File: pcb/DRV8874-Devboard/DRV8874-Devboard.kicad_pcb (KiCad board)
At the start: 4 copper layers, 65 x 67 mm, 57 parts, among them J1 Conn_01x04_Pin, J10 Conn_01x06_Pin, J12 Conn_01x03_Pin, J2 Screw_Terminal_01x02, J3 Conn_01x03_Pin, J4 Conn_01x03_Pin, J5 Conn_01x04_Pin, J6 Conn_01x03_Pin, J7 Conn_01x03_Pin, J8 Conn_01x03_Pin, J9 Conn_01x03_Pin, U1 DRV8874, U2 BL9342, U3 DRV8874, U4 SN65HVD230, U5 TPS16630PWPR, U6 M95320-WMN6TP, U7 TinyThinker_J1

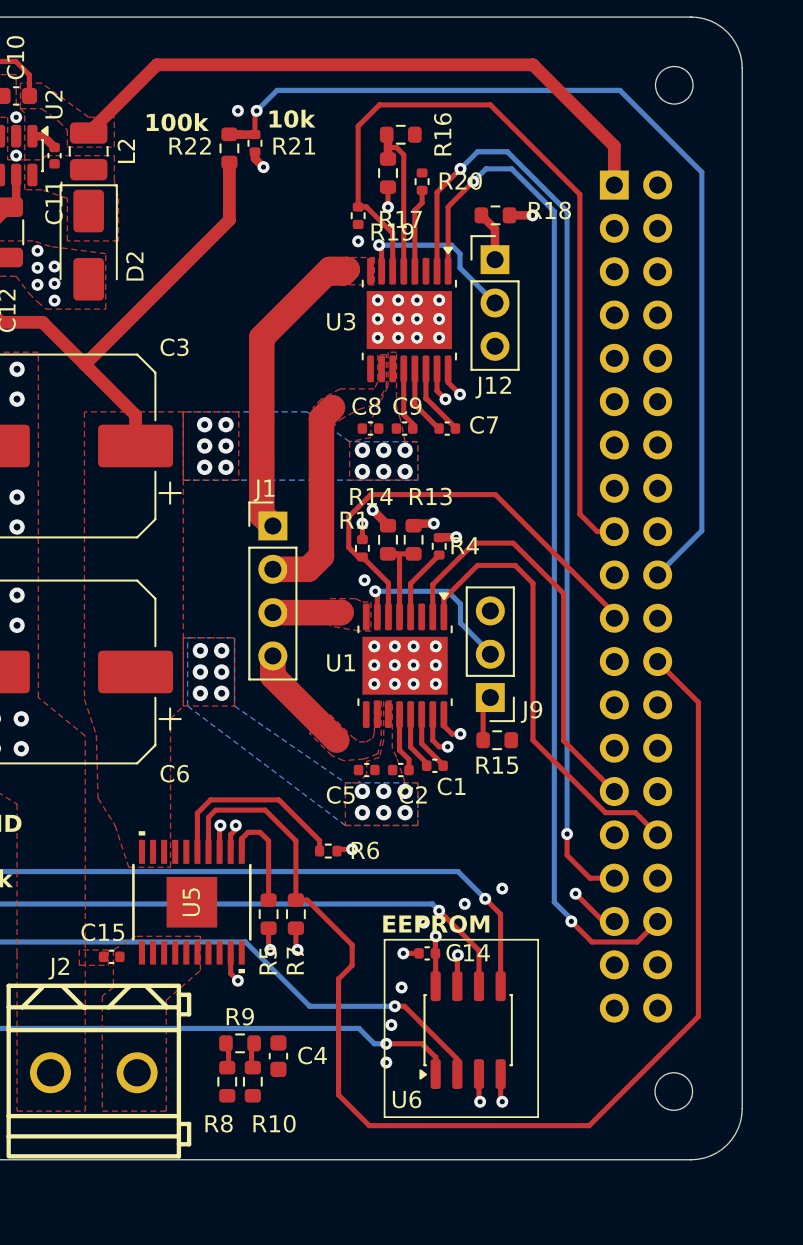
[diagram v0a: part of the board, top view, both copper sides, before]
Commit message: minor routing changes
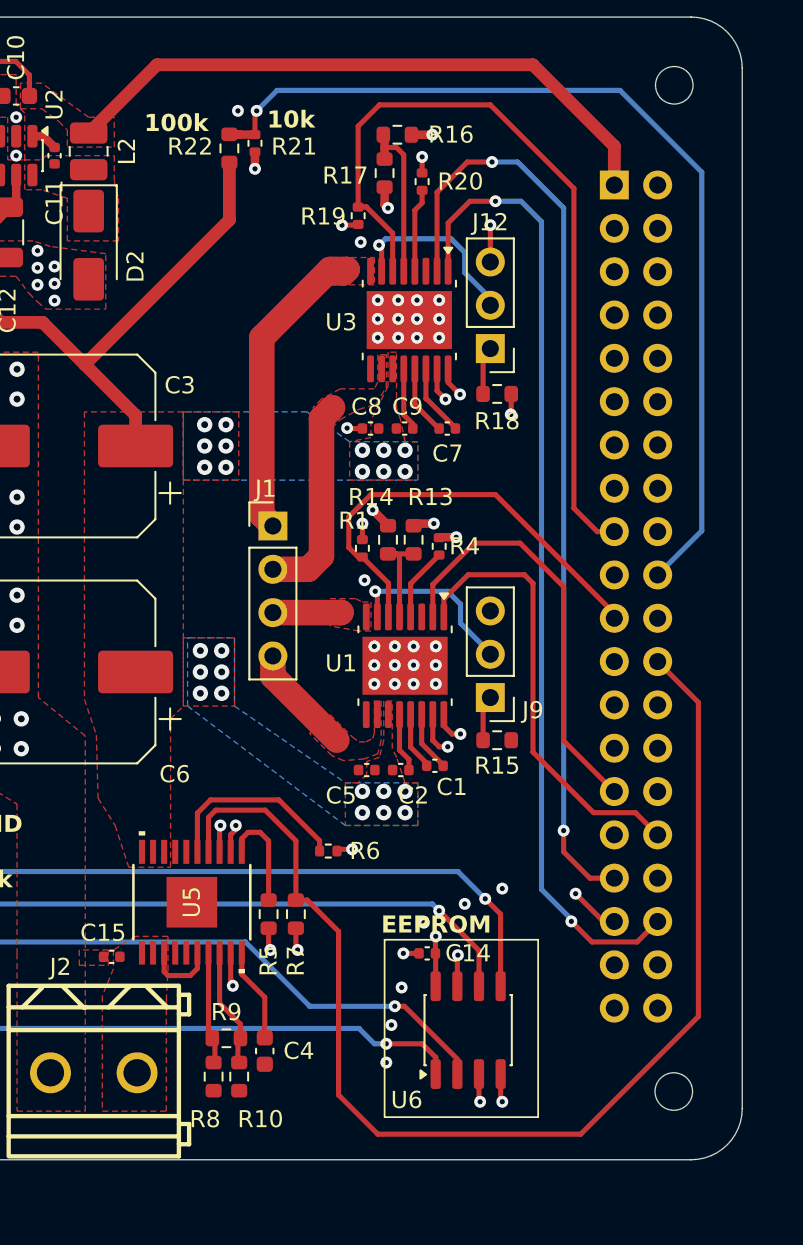
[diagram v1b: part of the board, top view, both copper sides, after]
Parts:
- moved R18 10.5 mm to (147.4, 61.7)
- moved J12 5.22 mm to (147.0, 59.0), turned to 180 degrees
- moved C4 0.85 mm to (133.8, 100.2)
- moved R10 0.85 mm to (132.3, 101.7)
- moved R8 0.85 mm to (130.8, 101.7)
- moved R9 0.85 mm to (131.5, 99.5)
- moved R16 0.20 mm to (141.6, 46.5)
- moved R17 0.20 mm to (140.8, 48.8)
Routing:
- net /TPS_DVDT: track 0.00 -> 5.56 mm
- net /TPS_OVP: track 1.56 -> 7.09 mm
- net /TPS_UVLO: track 1.85 -> 6.68 mm
- net +BATT_RAW: track 0.00 -> 4.27 mm
- net GND: track 29.0 -> 33.0 mm, vias 91 -> 94
- net /B_IN1: track 60.1 -> 57.1 mm
- net +3.3V: track 16.7 -> 18.8 mm, vias 10 -> 12
- net /B_IMODE: track 10.3 -> 10.8 mm

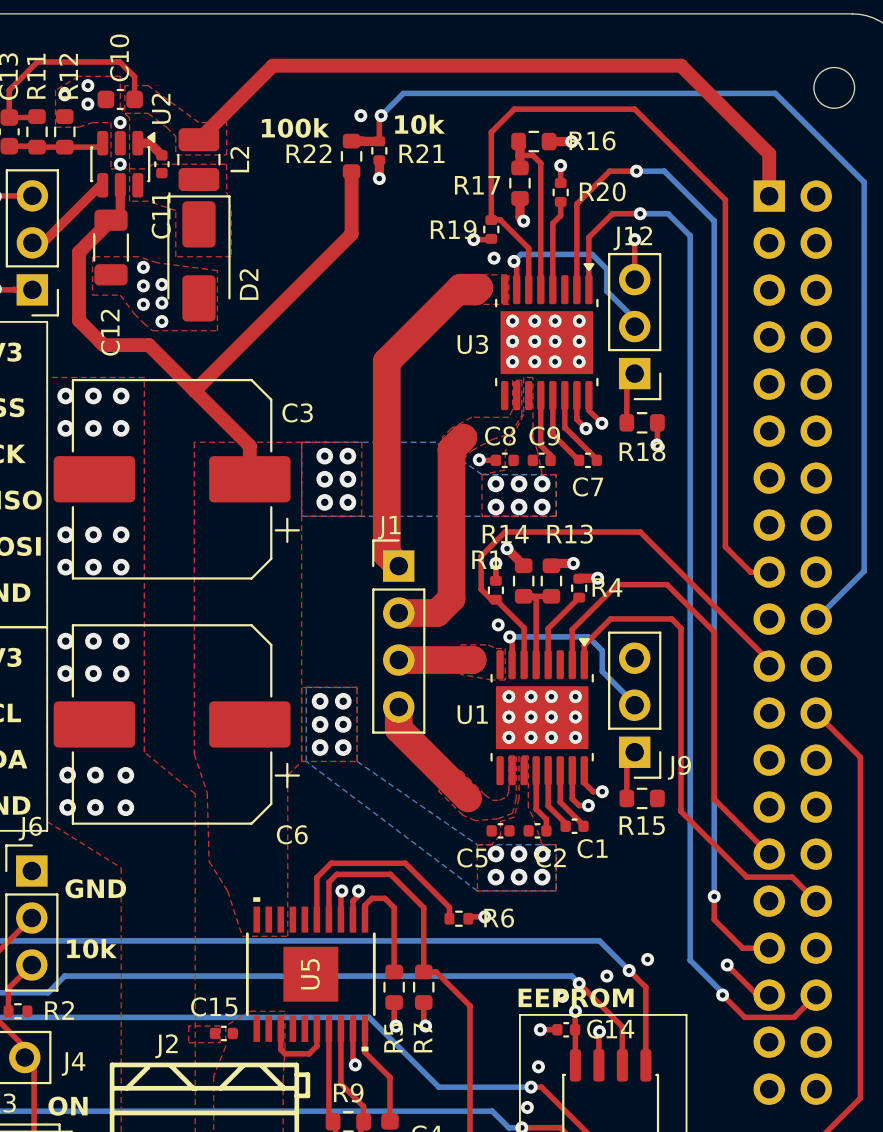
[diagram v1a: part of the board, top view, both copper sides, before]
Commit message: minor routing changes
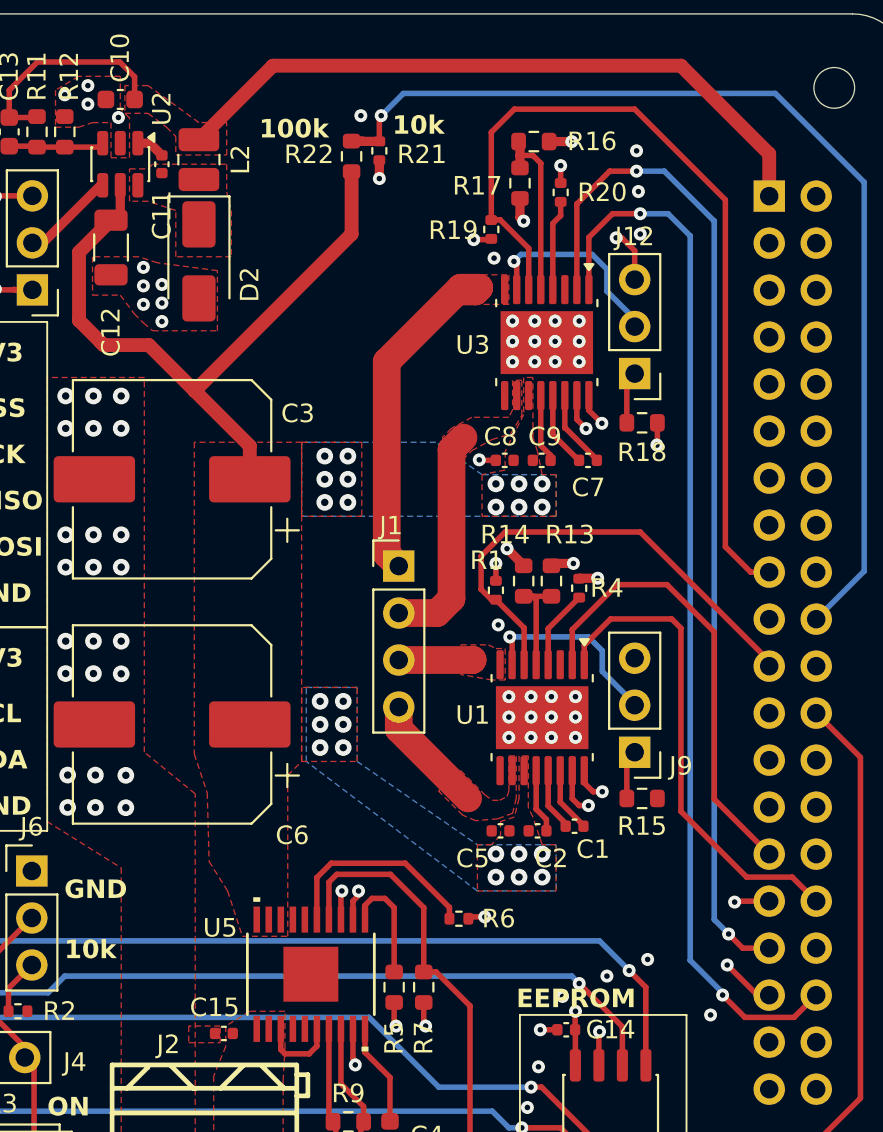
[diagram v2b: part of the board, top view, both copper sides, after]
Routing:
- net GND: track 33.0 -> 35.6 mm, vias 94 -> 98
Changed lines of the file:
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@@
 		(tags "TPS16630PWPR ")
 		(property "Reference" "U5"
-			(at 0 0 90)
+			(at 2.5 -4.9 0)
 			(unlocked yes)
 			(layer "F.SilkS")
@@
 	)
 	(segment
-		(start 147 53.96)
-		(end 147 51.8)
-		(width 0.3)
-		(layer "F.Cu")
-		(net 2)
-	)
-	(segment
 		(start 114.45 54.515)
 		(end 112.49 54.515)
@@
 	)
 	(segment
+		(start 146 51.7)
+		(end 146.3 51.7)
+		(width 0.3)
+		(layer "F.Cu")
+		(net 2)
+	)
+	(segment
 		(start 112 102)
 		(end 111.25 102.75)
@@
 	)
 	(segment
+		(start 152.45 87.55)
+		(end 152.4 87.6)
+		(width 0.3)
+		(layer "F.Cu")
+		(net 2)
+	)
+	(segment
 		(start 143.625 82.01)
 		(end 143.625 80.4975)
@@
 	)
 	(segment
+		(start 154.27 87.55)
+		(end 152.45 87.55)
+		(width 0.3)
+		(layer "F.Cu")
+		(net 2)
+	)
+	(segment
 		(start 113.49 54.515)
 		(end 113.45 54.475)
@@
 	)
 	(segment
+		(start 146.3 51.7)
+		(end 147 52.4)
+		(width 0.3)
+		(layer "F.Cu")
+		(net 2)
+	)
+	(segment
+		(start 147 52.4)
+		(end 147 53.96)
+		(width 0.3)
+		(layer "F.Cu")
+		(net 2)
+	)
+	(segment
 		(start 143.875 61.515923)
 		(end 144.371183 62.012106)
@@
 	)
 	(via
+		(at 152.4 87.6)
+		(size 0.7)
+		(drill 0.3)
+		(layers "F.Cu" "B.Cu")
+		(net 2)
+	)
+	(via
 		(at 119.5 82.5)
 		(size 0.9)
@@
 	)
 	(via
+		(at 151.1 93.7)
+		(size 0.7)
+		(drill 0.3)
+		(layers "F.Cu" "B.Cu")
+		(net 2)
+	)
+	(via
 		(at 138.3 51.8)
 		(size 0.7)
@@
 	)
 	(via
+		(at 147.2 49.2)
+		(size 0.7)
+		(drill 0.3)
+		(layers "F.Cu" "B.Cu")
+		(net 2)
+	)
+	(via
 		(at 152 91)
 		(size 0.7)
@@
 	)
 	(via
+		(at 147.3 51.5)
+		(size 0.7)
+		(drill 0.3)
+		(layers "F.Cu" "B.Cu")
+		(net 2)
+	)
+	(via
 		(at 144 57.3)
 		(size 0.7)
@@
 	)
 	(via
+		(at 147.1 47)
+		(size 0.7)
+		(drill 0.3)
+		(layers "F.Cu" "B.Cu")
+		(net 2)
+	)
+	(via
 		(at 142.7 58.4)
 		(size 0.7)
@@
 	)
 	(via
-		(at 119.2 45.475)
+		(at 119.1 45.2)
 		(size 0.7)
 		(drill 0.3)
@@
 	)
 	(via
-		(at 147 51.8)
+		(at 146 51.7)
 		(size 0.7)
 		(drill 0.3)
@@
 	)
 	(via
-		(at 119.2 47.725)
-		(size 0.7)
-		(drill 0.3)
-		(layers "F.Cu" "B.Cu")
-		(free yes)
-		(net 2)
-	)
-	(via
 		(at 119.25 73.5)
 		(size 0.9)
@@
 	)
 	(segment
-		(start 151.3 88.55)
-		(end 152.84 90.09)
-		(width 0.3)
-		(layer "F.Cu")
-		(net 64)
-	)
-	(segment
 		(start 152.84 90.09)
 		(end 154.27 90.09)
@@
 	)
 	(segment
-		(start 151.3 87.3)
-		(end 151.3 88.55)
+		(start 145.65 48.1)
+		(end 143.875 49.875)
 		(width 0.3)
 		(layer "F.Cu")
@@
 	)
 	(segment
-		(start 145.65 48.1)
-		(end 143.875 49.875)
+		(start 152.075 89.325)
+		(end 152.84 90.09)
 		(width 0.3)
 		(layer "F.Cu")
@@
 	)
 	(via
-		(at 151.3 87.3)
+		(at 152.075 89.325)
 		(size 0.7)
 		(drill 0.3)
@@
 	)
 	(segment
-		(start 147.1 48.1)
-		(end 148.6 48.1)
+		(start 152.075 89.325)
+		(end 151.3 88.55)
 		(width 0.3)
 		(layer "B.Cu")
@@
 	(segment
 		(start 148.6 48.1)
+		(end 147.1 48.1)
+		(width 0.3)
+		(layer "B.Cu")
+		(net 64)
+	)
+	(segment
+		(start 151.3 88.55)
 		(end 151.3 50.8)
 		(width 0.3)
@@
 	(segment
 		(start 151.3 50.8)
-		(end 151.3 87.3)
+		(end 148.6 48.1)
 		(width 0.3)
 		(layer "B.Cu")
@@
 		(polygon
 			(pts
-				(xy 118.7 47.975) (xy 119.7 47.975) (xy 119.7 45.225) (xy 119.2 44.725) (xy 119.2 42.975) (xy 116.95 42.975)
+				(xy 118.7 47.375) (xy 119.7 47.375) (xy 119.7 45.225) (xy 119.2 44.725) (xy 119.2 42.975) (xy 116.95 42.975)
 				(xy 115.7 43.725) (xy 115.7 45.725) (xy 116.95 45.725) (xy 117.7 45.475) (xy 118.7 45.475)
 			)

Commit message: more minor routing cleanup
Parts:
- moved R6 0.83 mm to (137.1, 89.2)
- moved R19 0.78 mm to (138.7, 50.7), turned to 180 degrees
- moved R13 0.55 mm to (142.5, 69.7)
- moved R4 0.39 mm to (143.8, 70.3)
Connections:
- U7 pad 12: unconnected-(U7A-TIM3_CH1-Pad12) -> /A_IN1
- U7 pad 29: /A_IN2 -> unconnected-(U7A-TIM2_CH4-Pad29)
- U7 pad 32: /A_IN1 -> unconnected-(U7A-TIM2_CH1-Pad32)
- U7 pad 33: /B_IN2 -> unconnected-(U7A-TIM2_CH2-Pad33)
- U7 pad 36: /B_IN1 -> unconnected-(U7A-TIM2_CH3-Pad36)
- U7 pad 5: unconnected-(U7A-TIM3_CH4-Pad5) -> /B_IN2
- U7 pad 8: unconnected-(U7A-TIM3_CH3-Pad8) -> /B_IN1
- U7 pad 9: unconnected-(U7A-TIM3_CH2-Pad9) -> /A_IN2
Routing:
- net GND: track 35.6 -> 93.8 mm, vias 98 -> 140
- net /B_IN1: track 57.1 -> 18.4 mm
- net /B_IN2: track 55.3 -> 19.2 mm
- net +3.3V: track 18.8 -> 51.9 mm, vias 12 -> 30
- net /A_IN1: track 26.3 -> 21.2 mm, vias 0 -> 2
- net +BATT_RAW: track 4.27 -> 9.19 mm
- net /A_IN2: track 24.9 -> 20.6 mm, vias 0 -> 2
- net /A_IMODE: track 10.5 -> 13.4 mm
- net /B_IPROPI: track 46.3 -> 48.7 mm
- net /ADC_VSENSE: track 56.7 -> 58.6 mm
- net /TPS_MON: track 71.2 -> 72.3 mm

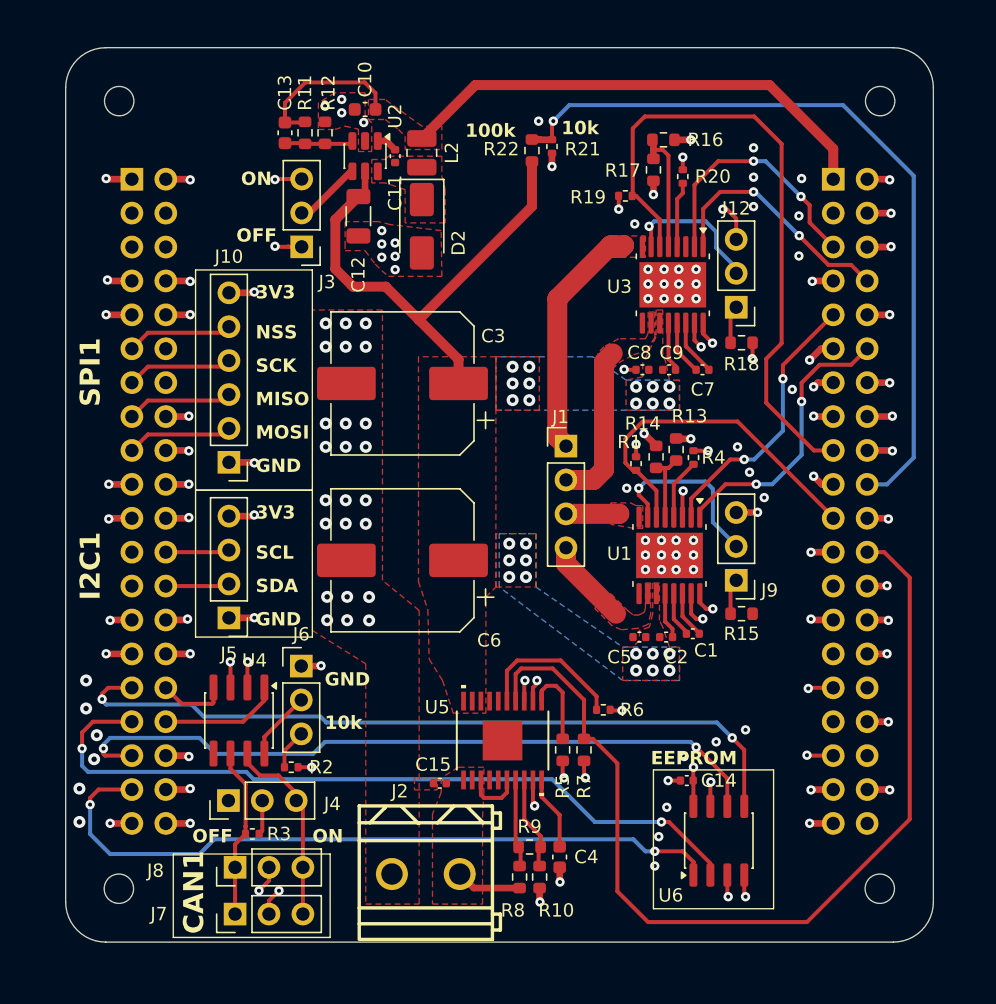
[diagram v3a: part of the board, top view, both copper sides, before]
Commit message: added 4 WS2812B RGB LEDs for status codes
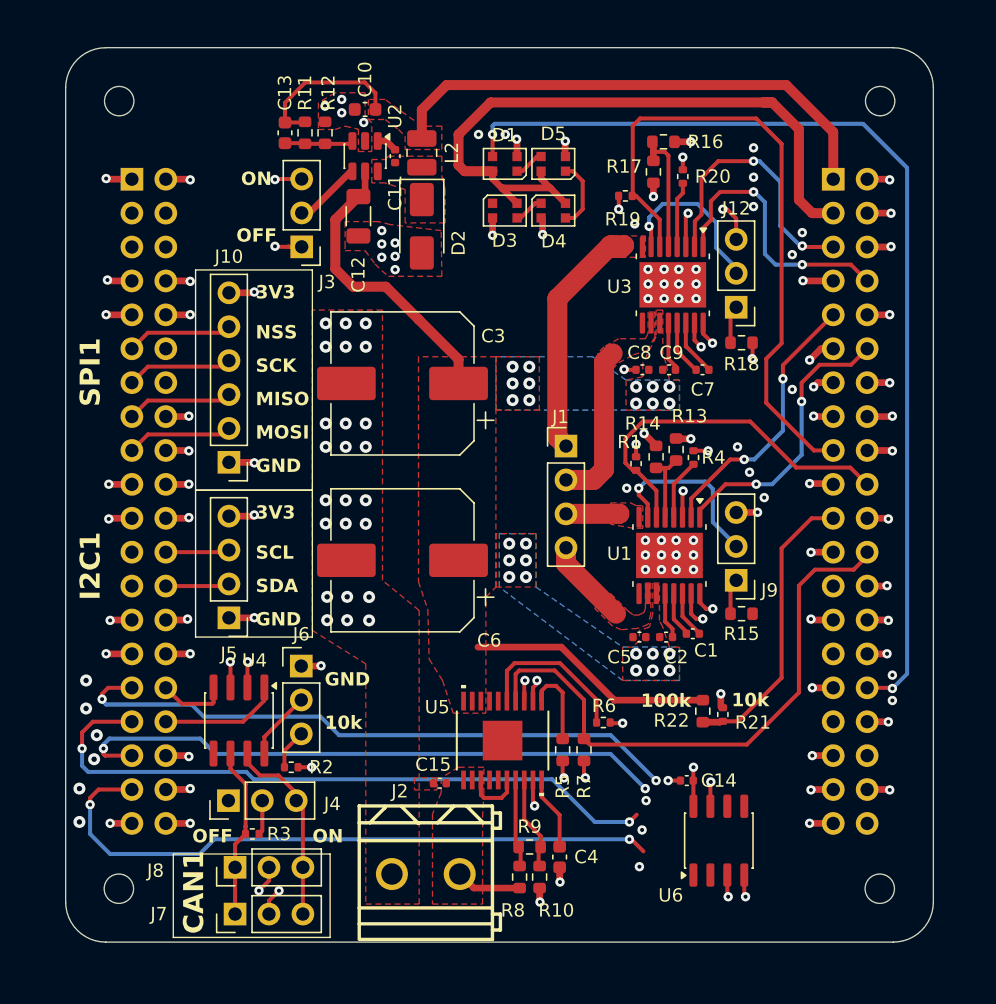
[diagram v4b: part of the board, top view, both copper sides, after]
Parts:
- added D1: WS2812B-2020, LED_SMD:LED_WS2812B-2020_PLCC4_2.0x2.0mm, F.Cu at (129.7, 48.3)
- added D3: WS2812B-2020, LED_SMD:LED_WS2812B-2020_PLCC4_2.0x2.0mm, F.Cu at (129.7, 51.8)
- added D4: WS2812B-2020, LED_SMD:LED_WS2812B-2020_PLCC4_2.0x2.0mm, F.Cu at (133.3, 51.8)
- added D5: WS2812B-2020, LED_SMD:LED_WS2812B-2020_PLCC4_2.0x2.0mm, F.Cu at (133.3, 48.3)
- moved R21 44.4 mm to (146.0, 89.5), turned to 90 degrees
- moved R22 43.9 mm to (144.5, 89.3), turned to -90 degrees
- moved R6 0.95 mm to (137.1, 90.2)
- moved R16 0.15 mm to (141.6, 46.6)
- moved R17 0.15 mm to (140.8, 48.9)
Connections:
- net +5V renamed +5V_EXT
- U7 pad 20: /ADC_VSENSE -> /A_IPROPI
- U7 pad 21: /A_IPROPI -> /ADC_VSENSE
- U7 pad 3: unconnected-(U7A-+5V_SYS-Pad3) -> +5V_SYS
- U7 pad 32: unconnected-(U7A-TIM2_CH1-Pad32) -> /RGB_LED_PWM
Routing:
- net /RGB_LED_PWM: track 0.00 -> 76.1 mm, vias 0 -> 2
- net +5V_SYS: track 0.00 -> 51.3 mm
- net /ADC_VSENSE: track 58.6 -> 21.7 mm, vias 1 -> 0
- net /TPS_MON: track 72.3 -> 43.4 mm
- net /SPI2_MOSI: track 56.8 -> 46.9 mm
- net /SPI2_SCK: track 53.9 -> 45.2 mm
- net /SPI2_MISO: track 57.5 -> 50.1 mm
- net Net-(D4-DIN): track 0.00 -> 5.26 mm
- net /SPI2_NSS: track 54.0 -> 49.0 mm
- net GND: track 93.8 -> 98.8 mm, vias 140 -> 143
- net +BATT_PROT: track 37.3 -> 40.4 mm
- net +3.3V: track 51.9 -> 54.4 mm, vias 30 -> 31
- net Net-(D3-DIN): track 0.00 -> 2.48 mm
- net /B_IN1: track 18.4 -> 20.7 mm
- net Net-(D1-DOUT): track 0.00 -> 2.26 mm
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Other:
- board text removed: "EEPROM"

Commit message: minor routing
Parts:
- moved R20 4.58 mm to (146.8, 46.7), turned to 180 degrees
- moved R17 1.80 mm to (141.4, 47.2), turned to 90 degrees
- moved R16 1.55 mm to (143.0, 47.2), turned to -90 degrees
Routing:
- net /B_nFault: track 4.92 -> 9.76 mm
- net /B_VREF: track 9.48 -> 8.54 mm
- net /B_IMODE: track 12.7 -> 13.4 mm
